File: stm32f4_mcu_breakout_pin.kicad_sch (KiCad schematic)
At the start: 1 part

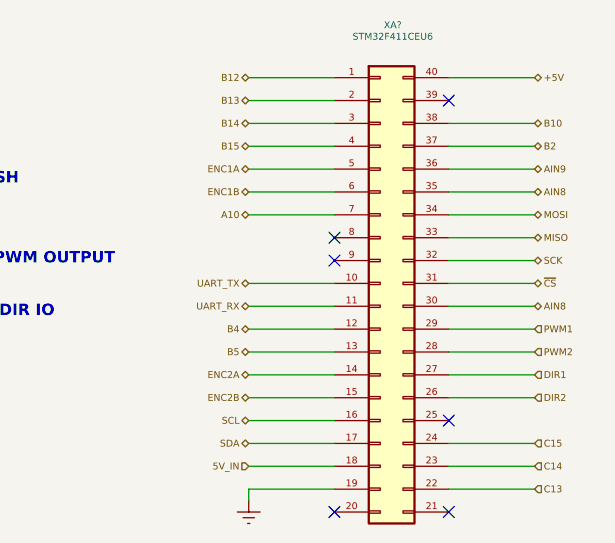
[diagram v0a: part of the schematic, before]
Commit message: Finished All footprints - PCB placement done momemtarily - plus wiring buck convertor done
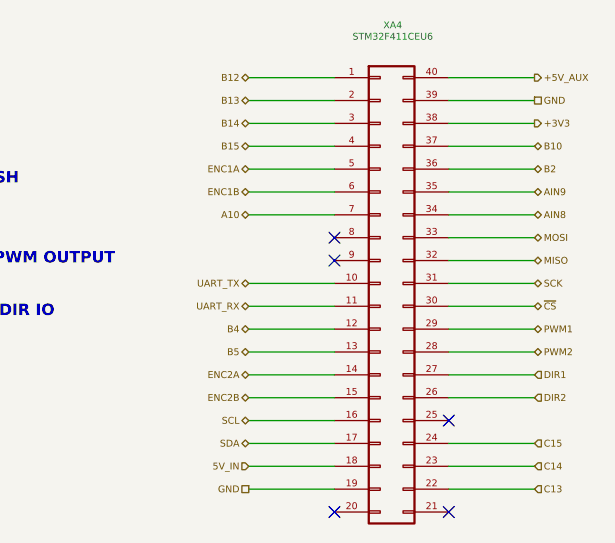
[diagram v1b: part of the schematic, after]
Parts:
- removed XA?: STM32F411CEU6, Connector_Samtec_HSEC8:Samtec_HSEC8-120-01-X-DV-A-WT_2x20_P0.8mm_Socket_WeldTabs, symbol Connector_Generic:Conn_02x20_Counter_Clockwise
- added XA4: STM32F411CEU6, Library:STM32F411_BlackPill_Socket, symbol Connector_Generic:Conn_02x20_Counter_Clockwise
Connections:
- net 5V_IN: now also XA4.18 (Pin_18)
- net A10: now also XA4.7 (Pin_7)
- net AIN8: now also XA4.34 (Pin_34)
- net AIN9: now also XA4.35 (Pin_35)
- net B10: now also XA4.37 (Pin_37)
- net B12: now also XA4.1 (Pin_1)
- net B13: now also XA4.2 (Pin_2)
- net B14: now also XA4.3 (Pin_3)
- net B15: now also XA4.4 (Pin_4)
- net B2: now also XA4.36 (Pin_36)
- net B4: now also XA4.12 (Pin_12)
- net B5: now also XA4.13 (Pin_13)
- net C13: now also XA4.22 (Pin_22)
- net C14: now also XA4.23 (Pin_23)
- net C15: now also XA4.24 (Pin_24)
- net DIR1: now also XA4.27 (Pin_27)
- net DIR2: now also XA4.26 (Pin_26)
- net ENC1A: now also XA4.5 (Pin_5)
- net ENC1B: now also XA4.6 (Pin_6)
- net ENC2A: now also XA4.14 (Pin_14)
- net ENC2B: now also XA4.15 (Pin_15)
- net MISO: now also XA4.32 (Pin_32)
- net MOSI: now also XA4.33 (Pin_33)
- net PWM1: now also XA4.29 (Pin_29)
- net PWM2: now also XA4.28 (Pin_28)
- net SCK: now also XA4.31 (Pin_31)
- net SCL: now also XA4.16 (Pin_16)
- net SDA: now also XA4.17 (Pin_17)
- net UART_RX: now also XA4.11 (Pin_11)
- net UART_TX: now also XA4.10 (Pin_10)
- net ~{CS}: now also XA4.30 (Pin_30)
- new net +3V3: XA4.38 (Pin_38)
- new net +5V_AUX: XA4.40 (Pin_40)
- new net GND: XA4.19 (Pin_19), XA4.39 (Pin_39)
- no-connect marks 6 -> 5

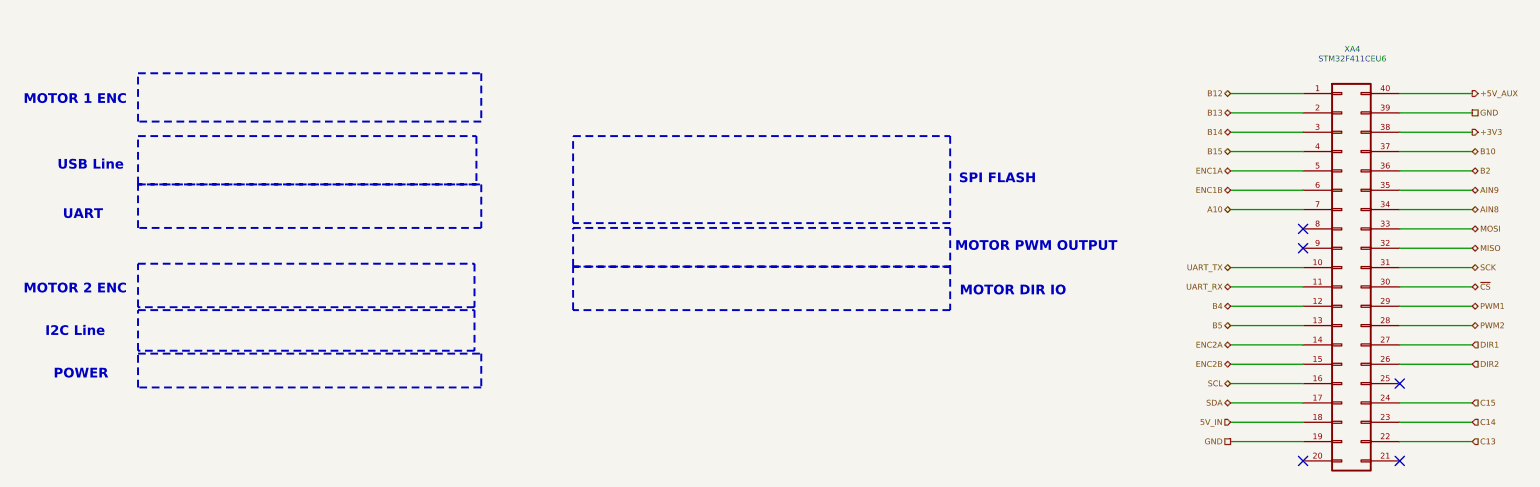
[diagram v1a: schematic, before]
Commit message: Changed TOF Trigger pins to B12-14 - also removed 3V3 access as board space are running out
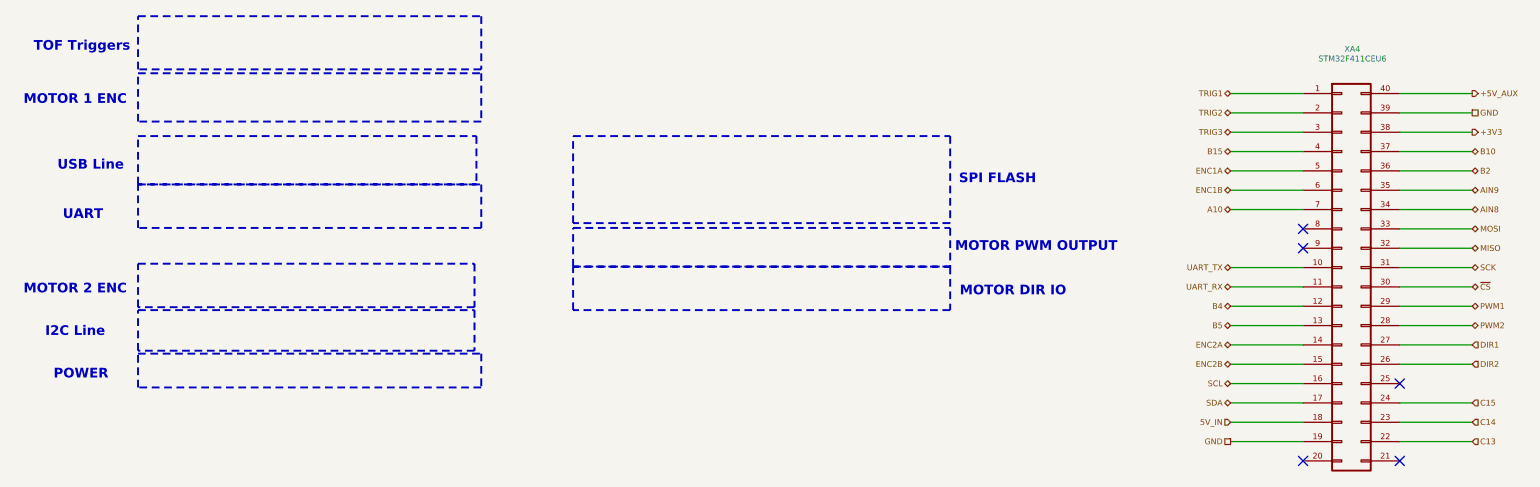
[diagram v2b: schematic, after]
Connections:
- net B12 renamed TRIG1
- net B13 renamed TRIG2
- net B14 renamed TRIG3
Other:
- note added: "TOF Triggers"
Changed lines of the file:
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@@
 	)
 	(rectangle
+		(start 43.18 57.15)
+		(end 88.265 64.135)
+		(stroke
+			(width 0.254)
+			(type dash)
+			(color 250 24 255 1)
+		)
+		(fill
+			(type none)
+		)
+	)
+	(rectangle
 		(start 43.18 72.898)
 		(end 87.63 79.248)
@@
 		)
 	)
+	(text "TOF Triggers"
+		(exclude_from_sim yes)
+		(at 35.814 61.214 0)
+		(effects
+			(font
+				(size 1.27 1.27)
+				(thickness 0.254)
+				(bold yes)
+				(color 255 32 255 1)
+			)
+		)
+	)
 	(text "USB Line"
 		(exclude_from_sim yes)
@@
 		)
 	)
-	(hierarchical_label "B13"
-		(shape bidirectional)
-		(at 186.69 69.85 180)
-		(effects
-			(font
-				(size 0.762 0.762)
-			)
-			(justify right)
-		)
-	)
 	(hierarchical_label "DIR1"
 		(shape input)
@@
 		)
 	)
-	(hierarchical_label "B14"
-		(shape bidirectional)
-		(at 186.69 72.39 180)
-		(effects
-			(font
-				(size 0.762 0.762)
-			)
-			(justify right)
-		)
-	)
 	(hierarchical_label "C14"
 		(shape input)
@@
 		)
 	)
-	(hierarchical_label "B12"
-		(shape bidirectional)
-		(at 186.69 67.31 180)
-		(effects
-			(font
-				(size 0.762 0.762)
-			)
-			(justify right)
-		)
-	)
 	(hierarchical_label "+3V3"
 		(shape output)
@@
 		)
 	)
+	(hierarchical_label "TRIG1"
+		(shape bidirectional)
+		(at 186.69 67.31 180)
+		(effects
+			(font
+				(size 0.762 0.762)
+			)
+			(justify right)
+		)
+	)
 	(hierarchical_label "PWM2"
 		(shape bidirectional)
@@
 		)
 	)
+	(hierarchical_label "TRIG2"
+		(shape bidirectional)
+		(at 186.69 69.85 180)
+		(effects
+			(font
+				(size 0.762 0.762)
+			)
+			(justify right)
+		)
+	)
 	(hierarchical_label "PWM1"
 		(shape bidirectional)
@@
 		)
 	)
+	(hierarchical_label "TRIG3"
+		(shape bidirectional)
+		(at 186.69 72.39 180)
+		(effects
+			(font
+				(size 0.762 0.762)
+			)
+			(justify right)
+		)
+	)

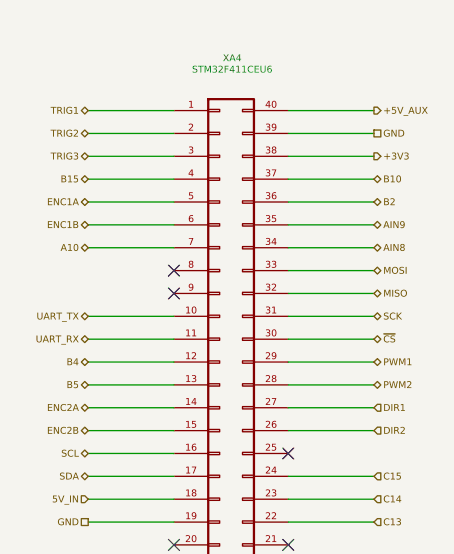
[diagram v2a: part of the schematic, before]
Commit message: Finialized and Finished PCB routing
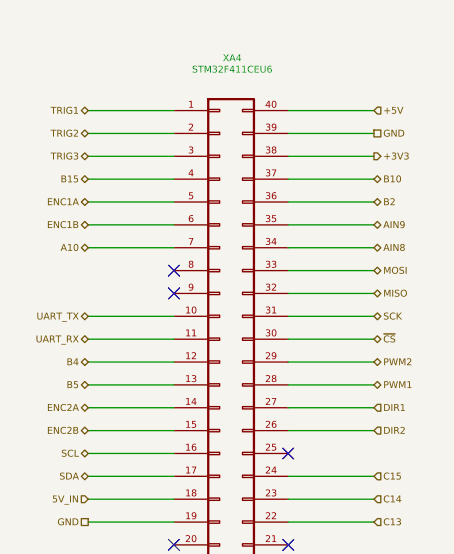
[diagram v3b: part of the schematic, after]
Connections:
- net PWM1: now also XA4.28 (Pin_28); no longer XA4.29 (Pin_29)
- net PWM2: now also XA4.29 (Pin_29); no longer XA4.28 (Pin_28)
- net +5V_AUX renamed +5V
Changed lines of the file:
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@@
-		)
-	)
-	(hierarchical_label "+5V_AUX"
-		(shape output)
-		(at 218.44 67.31 0)
-		(effects
-			(font
-				(size 0.762 0.762)
-			)
-			(justify left)
 		)
 	)
@@
 	(hierarchical_label "PWM2"
 		(shape bidirectional)
+		(at 218.44 95.25 0)
+		(effects
+			(font
+				(size 0.762 0.762)
+			)
+			(justify left)
+		)
+	)
+	(hierarchical_label "AIN8"
+		(shape bidirectional)
+		(at 218.44 82.55 0)
+		(effects
+			(font
+				(size 0.762 0.762)
+			)
+			(justify left)
+		)
+	)
+	(hierarchical_label "+5V"
+		(shape input)
+		(at 218.44 67.31 0)
+		(effects
+			(font
+				(size 0.762 0.762)
+			)
+			(justify left)
+		)
+	)
+	(hierarchical_label "TRIG2"
+		(shape bidirectional)
+		(at 186.69 69.85 180)
+		(effects
+			(font
+				(size 0.762 0.762)
+			)
+			(justify right)
+		)
+	)
+	(hierarchical_label "PWM1"
+		(shape bidirectional)
 		(at 218.44 97.79 0)
 		(effects
 			(font
-				(size 0.762 0.762)
-			)
-			(justify left)
-		)
-	)
-	(hierarchical_label "AIN8"
-		(shape bidirectional)
-		(at 218.44 82.55 0)
-		(effects
-			(font
-				(size 0.762 0.762)
-			)
-			(justify left)
-		)
-	)
-	(hierarchical_label "TRIG2"
-		(shape bidirectional)
-		(at 186.69 69.85 180)
-		(effects
-			(font
-				(size 0.762 0.762)
-			)
-			(justify right)
-		)
-	)
-	(hierarchical_label "PWM1"
-		(shape bidirectional)
-		(at 218.44 95.25 0)
-		(effects
-			(font
